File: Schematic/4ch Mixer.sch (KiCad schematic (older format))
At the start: 42 parts, among them J1 3.5mm_Mono_Jack_With_Switch, J2 3.5mm_Mono_Jack_With_Switch, J3 3.5mm_Mono_Jack_With_Switch, J4 3.5mm_Mono_Jack_With_Switch, J5 3.5mm_Mono_Jack_With_Switch, J6 3.5mm_Mono_Jack_With_Switch, P1 CONN_02X08, U1 TL074, U2 TL072

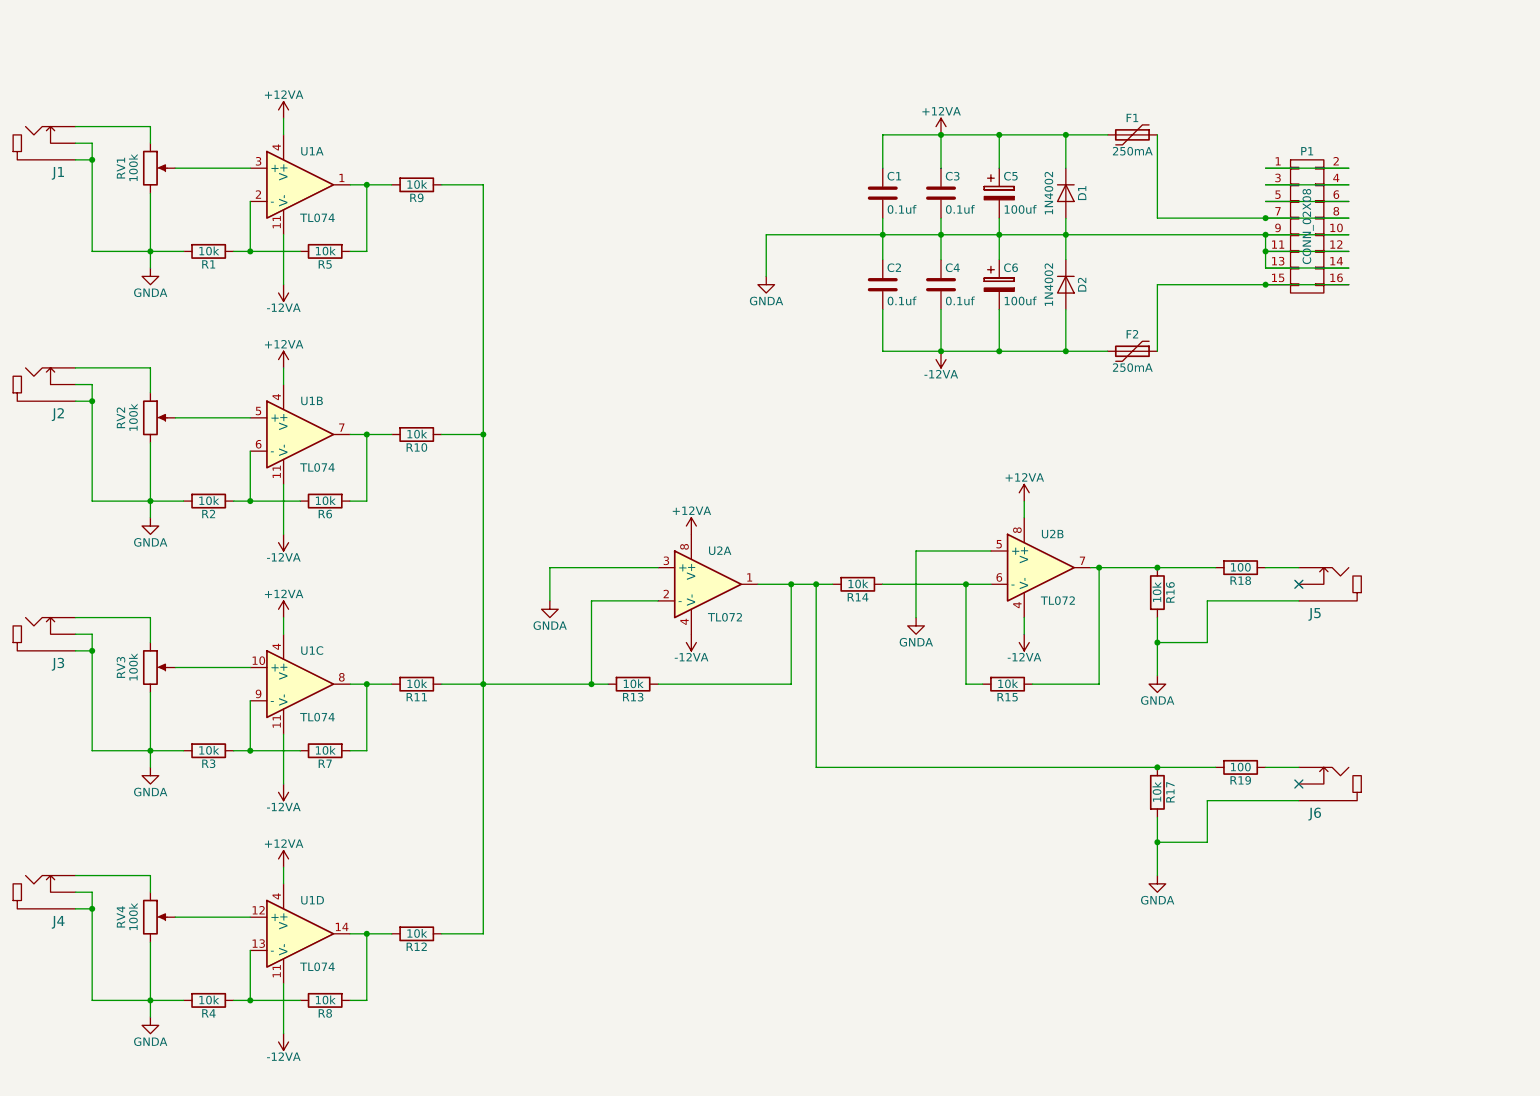
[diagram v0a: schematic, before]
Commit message: Build a new PCB layout with a smaller footprint
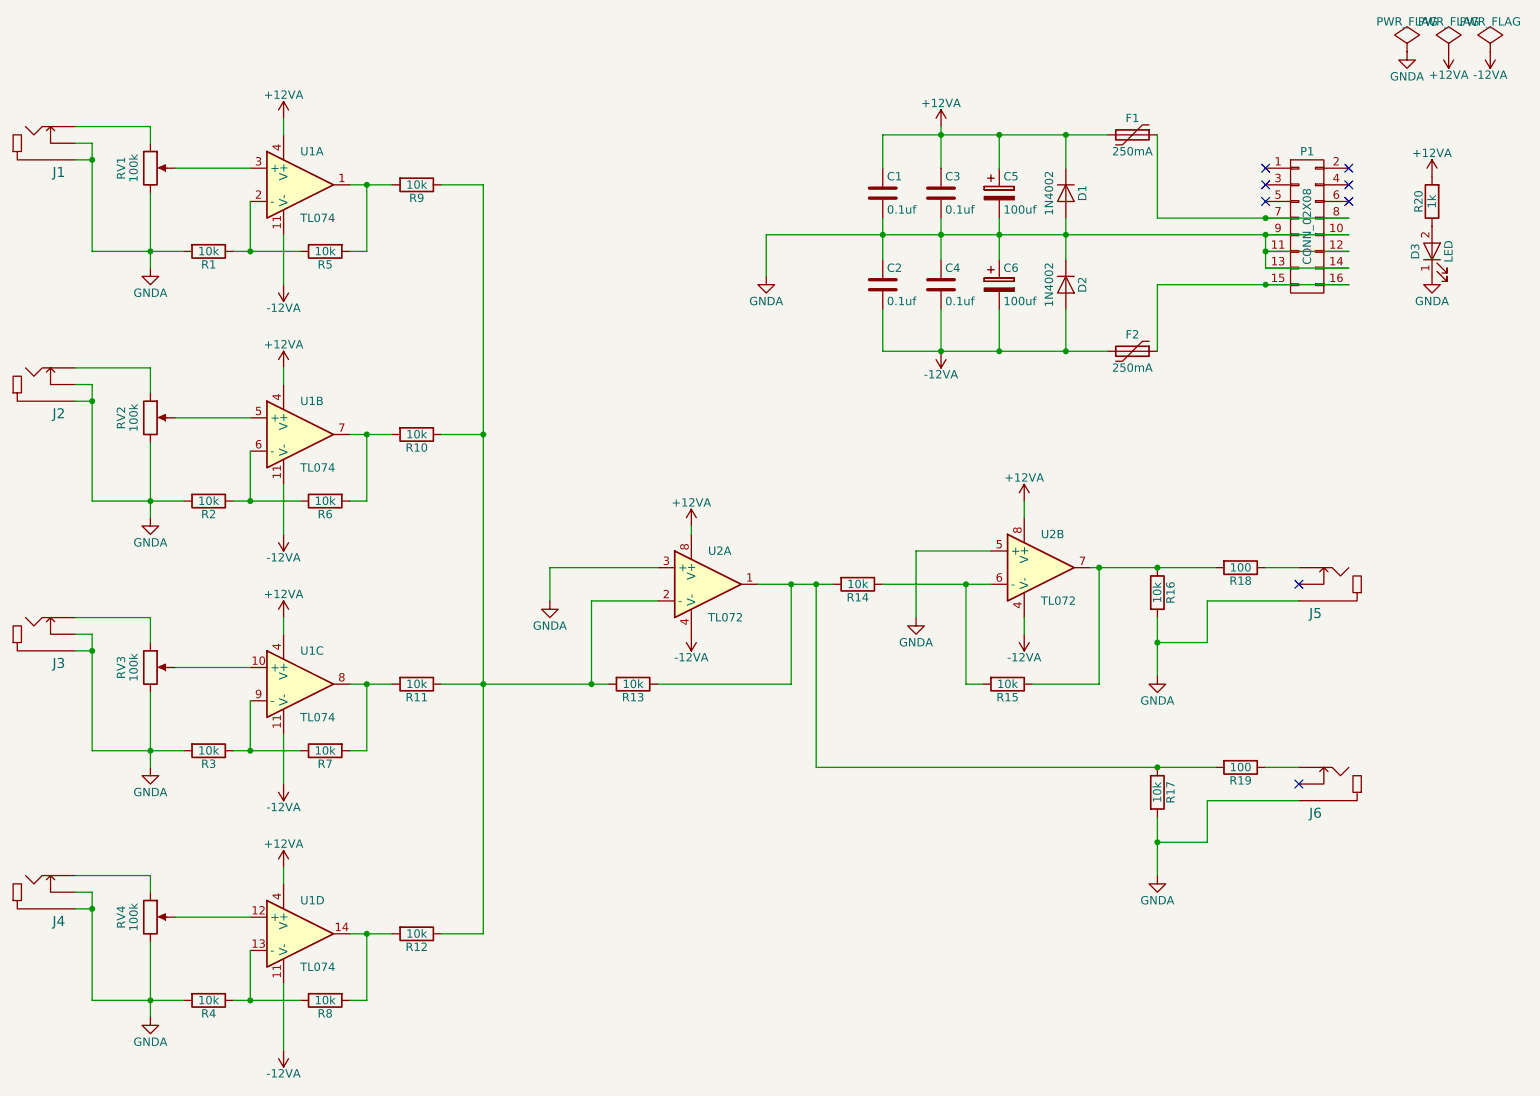
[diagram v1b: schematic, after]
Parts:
- added D3: LED, LEDs:LED_D3.0mm, symbol LED
- added R20: 1k, Resistors_THT:R_Axial_DIN0207_L6.3mm_D2.5mm_P2.54mm_Vertical, symbol R
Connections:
- net +12VA: now also R20.2
- net GNDA: now also D3.1 (K)
- net at P1.1 (P1): no longer P1.2 (P2)
- net at P1.3 (P3): no longer P1.4 (P4)
- net at P1.5 (P5): no longer P1.6 (P6)
- new net: D3.2 (A), R20.1
- no-connect marks 2 -> 8

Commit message: I think the board is done
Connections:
- net at R5.2, U1.1: now also R9.1; no longer R9.2
- net at R10.1, R11.1, R12.1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: now also R9.2; no longer R9.1
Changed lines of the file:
@@
 F 3 "" H 3800 1600 50  0000 C CNN
 	1    3800 1600
-	0    1    1    0
+	0    -1   1    0
 $EndComp
 $Comp

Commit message: Added caps to final op amp feedback.
Moved big bypass caps to backside of board.
Added mounting hole.
Generated new Gerbers
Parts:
- added C7, C8: 10pf, Capacitors_THT:C_Disc_D3.0mm_W2.0mm_P2.50mm, symbol C
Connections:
- net at R13.1, R14.2, R17.1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: now also C7.1
- net at R10.1, R11.1, R12.1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: now also C7.2
- net at R14.1, R15.2, U2.6 (-): now also C8.2
- net at R15.1, R16.1, R18.2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: now also C8.1
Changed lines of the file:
@@
 	5250 4600 6050 4600
 Wire Wire Line
-	6050 4600 6050 4000
+	6050 4000 6050 4850
 Wire Wire Line
 	5850 4000 6300 4000
@@
 	5250 4100 4850 4100
 Wire Wire Line
-	4850 4100 4850 4600
+	4850 4100 4850 4850
 Wire Wire Line
 	5250 3900 4600 3900
@@
 	7900 4600 7500 4600
 Wire Wire Line
-	7900 4600 7900 3900
-Wire Wire Line
-	7100 4000 7100 4600
+	7900 3900 7900 4850
+Wire Wire Line
+	7100 4000 7100 4850
 Connection ~ 7100 4000
 Wire Wire Line
@@
 Wire Wire Line
 	3000 6400 3000 6800
+$Comp
+L C C8
+U 1 1 58C17397
+P 7350 4850
+F 0 "C8" H 7375 4950 50  0000 L CNN
+F 1 "10pf" H 7375 4750 50  0000 L CNN
+F 2 "Capacitors_THT:C_Disc_D3.0mm_W2.0mm_P2.50mm" H 7388 4700 50  0001 C CNN
+F 3 "" H 7350 4850 50  0000 C CNN
+	1    7350 4850
+	0    1    1    0
+$EndComp
+Wire Wire Line
+	7900 4850 7500 4850
+Connection ~ 7900 4600
+Wire Wire Line
+	7100 4850 7200 4850
+Connection ~ 7100 4600
+$Comp
+L C C7
+U 1 1 58C17D77
+P 5100 4850
+F 0 "C7" H 5125 4950 50  0000 L CNN
+F 1 "10pf" H 5125 4750 50  0000 L CNN
+F 2 "Capacitors_THT:C_Disc_D3.0mm_W2.0mm_P2.50mm" H 5138 4700 50  0001 C CNN
+F 3 "" H 5100 4850 50  0000 C CNN
+	1    5100 4850
+	0    1    1    0
+$EndComp
+Wire Wire Line
+	6050 4850 5250 4850
+Connection ~ 6050 4600
+Wire Wire Line
+	4850 4850 4950 4850
 $EndSCHEMATC
